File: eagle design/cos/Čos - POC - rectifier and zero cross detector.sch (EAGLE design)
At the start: 42 parts, among them IC1 LT1716CS5#TRMPBF, IC2 LBA710S, IC3 LBA710S, Q1 DMN10H220L-7

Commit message: - removed .net file from LTSpice simulation - updated schematics, generated BOM, ERC checks out fine
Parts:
- added C6: 4700μF / 35V / ultralow ESR, C-Pol:C-POL
- R10: device rcl:R-EU_R0402 -> rcl:R-EU_R0805
- R3, R4, R5, R6: value 3k795 -> 760R
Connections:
- net GND: now also C6.NEG
- net V_REGULATED_TP2-IN: now also C6.POS
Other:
- note added: "647-UPW1V472MHD - 4700uF/35V 647-UHD1V471MPD - 470uF/35V 647-UHD1V331MPD - 330uF/35V 647-UHD1V221MPD6 - 220uF/35V 647-UHV1V151MPD - 150uF/35V"
- note added: "Bicycle Dynamo Grätz Bridge Rectifier / Delon Voltage Doubler w. zero cross detector"
- note added: "Dynamo AC rectified & smoothed to: 0V>Vdc>18V"
- note added: "Grätz/Delon conceptual overview"
- note added: "LED resistors & jumpers for manual switch actuation"
- note added: "Load, conceptual overview"
- note added: "Solid-State Relay switches"
- note added: "Uf=1.2V, If=5mA R=(5V-1.2V)/5mA=3.8V/0.005A=760 Ohm"
- note added: "any load, ideally: Buck/Boost converter Vin:0-18V Vout:5V0"
- note added: "form A (NO); datasheet p. 3 LED current ~0.8mA, Uf=1.235V"
- note added: "form B (NC); datasheet p. 5 LED current ~0.23mA, Uf=1.235V"
- note added: "jumpers for switch bypass"
- note added: "switching elements, optically actuated MOSFets"
- note added: "zero-cross signal requires 5V0 input for level translation"
- note removed: "0V> Vdc > 18V"
- note removed: "5V0"
- note removed: "647-UHD1V471MPD - 470uF/35V 647-UHD1V331MPD - 330uF/35V 647-UHD1V221MPD6 - 220uF/35V 647-UHV1V151MPD - 150uF/35V"
- note removed: "AC Rectifier with zero cross detector"
- note removed: "Buck-Boost Converter Vin = regulated AC Vout = 5V0"
- note removed: "Capacitor switches"
- note removed: "Dynamo AC regulated output"
- note removed: "GND"
- note removed: "Load"
- note removed: "conceptual overview"
- moved on the sheet: C1, C2, C3, C4, C5, D1, D2, D3, D4, D5, D6, D7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

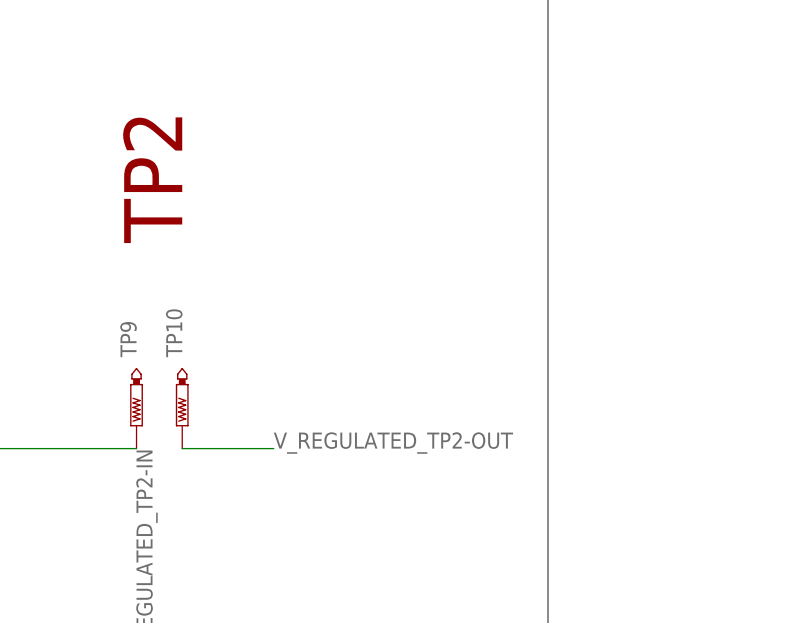
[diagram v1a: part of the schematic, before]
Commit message: - corrected netclasses
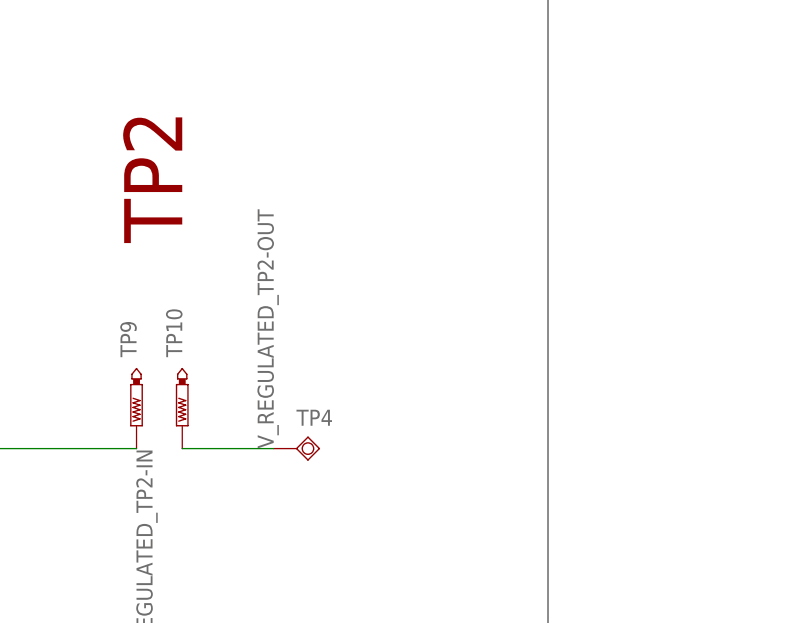
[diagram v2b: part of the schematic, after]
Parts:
- added TP4: Li-Ion Cell +, testpad:TPSQPAD1-13
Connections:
- net V_REGULATED_TP2-OUT: now also TP4.TP
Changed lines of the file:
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@@
 <clearance class="0" value="0.2"/>
 </class>
-<class number="1" name="GND_VIA_INCP" width="0.5" drill="0.3">
-<clearance class="1" value="0.2"/>
+<class number="1" name="DYNAMO_OUT" width="0.9" drill="0">
+<clearance class="1" value="0.5"/>
 </class>
-<class number="2" name="DYNAMO_OUT" width="0.9" drill="0.3">
-<clearance class="2" value="0.5"/>
+<class number="2" name="V_DC" width="0.3" drill="0.3">
+<clearance class="2" value="0.2"/>
 </class>
-<class number="3" name="V_DC" width="0.3" drill="0.3">
+<class number="3" name="V_REGULATED" width="0.3" drill="0.3">
 <clearance class="3" value="0.2"/>
 </class>
-<class number="4" name="V_REGULATED" width="0.3" drill="0.3">
+<class number="4" name="5V0" width="0.3" drill="0.3">
 <clearance class="4" value="0.2"/>
 </class>
-<class number="5" name="V_LI-ION" width="0.3" drill="0.3">
+<class number="5" name="signal" width="0.3" drill="0.3">
 <clearance class="5" value="0.2"/>
-</class>
-<class number="6" name="5V0" width="0.3" drill="0.3">
-<clearance class="6" value="0.2"/>
-</class>
-<class number="7" name="6V0" width="0.3" drill="0.3">
-<clearance class="7" value="0.2"/>
-</class>
-<class number="8" name="SOLAR-CELL" width="0.3" drill="0.3">
-<clearance class="8" value="0.2"/>
-</class>
-<class number="9" name="signal" width="0.3" drill="0.3">
-<clearance class="9" value="0.2"/>
-</class>
-<class number="10" name="LI_ION-CELL" width="0" drill="0">
 </class>
 </classes>
@@
 <part name="TP3" library="testpad" library_urn="urn:adsk.eagle:library:385" deviceset="TPSQ" device="PAD1-13" package3d_urn="urn:adsk.eagle:package:27946/1" value="Li-Ion Cell +"/>
 <part name="C6" library="C-Pol" deviceset="C-POL" device="" value="4700μF / 35V / ultralow ESR"/>
+<part name="TP4" library="testpad" library_urn="urn:adsk.eagle:library:385" deviceset="TPSQ" device="PAD1-13" package3d_urn="urn:adsk.eagle:package:27946/1" value="Li-Ion Cell +"/>
 </parts>
 <sheets>
@@
 <attribute name="VALUE" x="388.62" y="528.32" size="1.778" layer="96" rot="R90" align="center"/>
 </instance>
+<instance part="TP4" gate="G$1" x="429.26" y="548.64" smashed="yes" rot="R90">
+<attribute name="NAME" x="429.26" y="551.18" size="1.778" layer="95"/>
+<attribute name="TP_SIGNAL_NAME" x="430.53" y="551.18" size="1.778" layer="97" rot="R90"/>
+</instance>
 </instances>
 <busses>
@@
 </segment>
 </net>
-<net name="ZENER_COMMON" class="2">
+<net name="ZENER_COMMON" class="1">
 <segment>
 <pinref part="D2" gate="G$1" pin="C"/>
@@
 </segment>
 </net>
-<net name="DYNAMO2_GRAETZ" class="2">
+<net name="DYNAMO2_GRAETZ" class="1">
 <segment>
 <wire x1="218.44" y1="695.96" x2="218.44" y2="716.28" width="0.1524" layer="91"/>
@@
 </segment>
 </net>
-<net name="DYNAMO1" class="2">
+<net name="DYNAMO1" class="1">
 <segment>
 <pinref part="D4" gate="G$1" pin="C"/>
@@
 </segment>
 </net>
-<net name="DYNAMO2_BEFORE_TUNING-CAP_SW" class="2">
+<net name="DYNAMO2_BEFORE_TUNING-CAP_SW" class="1">
 <segment>
 <wire x1="152.4" y1="708.66" x2="144.78" y2="708.66" width="0.1524" layer="91"/>
@@
 </segment>
 </net>
-<net name="TUNING_CAP_BIAS" class="9">
+<net name="TUNING_CAP_BIAS" class="1">
 <segment>
 <pinref part="R10" gate="G$1" pin="1"/>
@@
 </segment>
 </net>
-<net name="DYNAMO2_DELON" class="2">
+<net name="DYNAMO2_DELON" class="1">
 <segment>
 <wire x1="289.56" y1="576.58" x2="279.4" y2="576.58" width="0.1524" layer="91"/>
@@
 <pinref part="TP10" gate="G$1" pin="TP"/>
 <wire x1="416.56" y1="548.64" x2="426.72" y2="548.64" width="0.1524" layer="91"/>
-<label x="426.72" y="548.64" size="1.778" layer="95"/>
+<label x="426.72" y="548.64" size="1.778" layer="95" rot="R90"/>
+<pinref part="TP4" gate="G$1" pin="TP"/>
 </segment>
 <segment>
@@
 </segment>
 </net>
-<net name="DYNAMO2_AFTER_TUNING-CAP_SW" class="2">
+<net name="DYNAMO2_AFTER_TUNING-CAP_SW" class="1">
 <segment>
 <wire x1="162.56" y1="708.66" x2="172.72" y2="708.66" width="0.1524" layer="91"/>
@@
 </segment>
 </net>
-<net name="DYNAMO2_BEFORE_G/D" class="2">
+<net name="DYNAMO2_BEFORE_G/D" class="1">
 <segment>
 <label x="190.5" y="716.28" size="0.8128" layer="95" rot="R90"/>
@@
 </segment>
 </net>
-<net name="ANODE_DELON" class="9">
+<net name="ANODE_DELON" class="5">
 <segment>
 <pinref part="IC3" gate="G$1" pin="3_ANODE2"/>
@@
 </segment>
 </net>
-<net name="ANODE_TUNING-CAP" class="9">
+<net name="ANODE_TUNING-CAP" class="5">
 <segment>
 <pinref part="IC2" gate="G$1" pin="3_ANODE2"/>
@@
 </segment>
 </net>
-<net name="ANODE_TUNING-CAP_BYPASS" class="9">
+<net name="ANODE_TUNING-CAP_BYPASS" class="5">
 <segment>
 <pinref part="IC2" gate="G$1" pin="1_ANODE1"/>
@@
 </segment>
 </net>
-<net name="ANODE_GRAETZ" class="9">
+<net name="ANODE_GRAETZ" class="5">
 <segment>
 <pinref part="IC3" gate="G$1" pin="1_ANODE1"/>
@@
 </segment>
 </net>
-<net name="OUT" class="0">
+<net name="OUT" class="5">
 <segment>
 <pinref part="IC1" gate="G$1" pin="1"/>
@@
 </segment>
 </net>
-<net name="ZEROCROSS" class="0">
+<net name="ZEROCROSS" class="5">
 <segment>
 <pinref part="Q1" gate="G$1" pin="S"/>
@@
 </segment>
 </net>
-<net name="5V0" class="0">
+<net name="5V0" class="4">
 <segment>
 <pinref part="Q1" gate="G$1" pin="G"/>
@@
 </segment>
 </net>
-<net name="N$4" class="0">
+<net name="N$4" class="5">
 <segment>
 <pinref part="R3" gate="G$1" pin="1"/>
@@
 </segment>
 </net>
-<net name="N$5" class="0">
+<net name="N$5" class="5">
 <segment>
 <pinref part="R4" gate="G$1" pin="1"/>
@@
 </segment>
 </net>
-<net name="N$6" class="0">
+<net name="N$6" class="5">
 <segment>
 <pinref part="R5" gate="G$1" pin="1"/>
@@
 </segment>
 </net>
-<net name="N$7" class="0">
+<net name="N$7" class="5">
 <segment>
 <pinref part="R6" gate="G$1" pin="1"/>

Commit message: - added SMD pads C-Pol.lbr library - 1st version of routed brd, ERC & DRC check out fine
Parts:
- added TP7, TP8: Li-Ion Cell +, testpad:TPSQPAD1-13
- C1, C2: value 330μF / 35V / ultralow ESR -> 3300μF / 35V / ultralow ESR; device C-Pol:C-POL -> C-Pol:C-POLSMD
- C3, C4: value 3300μF / 35V / ultralow ESR -> 330μF / 35V / ultralow ESR; device C-Pol:C-POL -> C-Pol:C-POLSMD
- C5, C6: device C-Pol:C-POL -> C-Pol:C-POLSMD
- TP1, TP2: value Li-Ion Cell + -> PTR1TP10SQ; device testpad:TPSQPAD1-13 -> testpad:PTR1TP10SQ
- TP10, TP9: value PTR1TP10SQ -> Li-Ion Cell +; device testpad:PTR1TP10SQ -> testpad:TPSQPAD1-13
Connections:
- net 5V0: now also JP5.1, JP6.1, TP7.TP; no longer JP1.1, JP2.1, TP3.TP
- net DYNAMO1: now also TP3.TP; no longer TP1.TP
- net DYNAMO2_AFTER_TUNING-CAP_SW: now also C1.NEG, JP2.1; no longer C3.NEG, JP6.1
- net DYNAMO2_BEFORE_G/D: now also C2.NEG, JP1.1; no longer C4.NEG, JP5.1
- net DYNAMO2_BEFORE_TUNING-CAP_SW: now also JP1.2, JP2.2, TP4.TP; no longer JP5.2, JP6.2, TP2.TP
- net DYNAMO2_DELON: now also C3.NEG, C4.POS; no longer C1.NEG, C2.POS
- net GND: now also C4.NEG, IC1.2_V-, TP10.TP; no longer C2.NEG, IC1.2
- net IN+: now also IC1.3_IN+; no longer IC1.3
- net IN-: now also IC1.4_IN-; no longer IC1.4
- net N$4: now also JP3.2; no longer JP1.2
- net N$5: now also JP4.2; no longer JP2.2
- net N$6: now also JP5.2; no longer JP3.2
- net N$7: now also JP6.2; no longer JP4.2
- net OUT: now also IC1.1_OUT; no longer IC1.1
- net TUNING_CAP_BIAS: now also C1.POS, C2.POS; no longer C3.POS, C4.POS
- net V_RECT_TP1-IN: now also C3.POS, TP1.TP; no longer C1.POS, TP5.TP
- net V_RECT_TP1-OUT: now also TP2.TP; no longer TP6.TP
- net V_REGULATED_TP2-IN: now also IC1.5_V+, TP5.TP; no longer IC1.5, TP9.TP
- net V_REGULATED_TP2-OUT: now also TP6.TP, TP9.TP; no longer TP10.TP, TP4.TP
- net ZEROCROSS: now also TP8.TP
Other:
- note added: "C5 / C6"
- note added: "D6"
- note removed: "C5"
- moved on the sheet: C1, C2, C3, C4, JP1, JP2, JP3, JP4, JP5, JP6, TP3, TP4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

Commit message: HW rev. 1 - finished routing, specified BOM, created gerbers
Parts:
- removed JP1, JP2, JP7, JP8: (no value), jumper:JP1Q
- added SW1_NC, SW2_NO, SW3_NC, SW4_NO: (no value), jumper:JP1Q
- renumbered JP3 to TCAP_BYPASS, JP4 to TCAP, JP5 to GRAETZ, JP6 to DELON, TP10 to GND, TP3 to DYN1, TP4 to DYN2, TP7 to 5V0, TP8 to ZC, TP9 to VREG
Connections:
- net DYNAMO2_AFTER_TUNING-CAP_SW: now also SW2_NO.1; no longer JP2.1
- net DYNAMO2_BEFORE_G/D: now also SW1_NC.1, SW3_NC.2, SW4_NO.2; no longer JP1.1, JP7.2, JP8.2
- net DYNAMO2_BEFORE_TUNING-CAP_SW: now also SW1_NC.2, SW2_NO.2; no longer JP1.2, JP2.2
- net DYNAMO2_DELON: now also SW4_NO.1; no longer JP8.1
- net DYNAMO2_GRAETZ: now also SW3_NC.1; no longer JP7.1
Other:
- note added: "647-UPW1V472MHD - 4700uF/35V 647-UHE1V332MHD6 - 3300uF/35V 647-UHD1V471MPD - 470uF/35V 647-UHD1V331MPD - 330uF/35V 647-UHD1V221MPD6 - 220uF/35V 647-UHV1V151MPD - 150uF/35V"
- note added: "jumpers for solid state relay override"
- note removed: "647-UPW1V472MHD - 4700uF/35V 647-UHD1V471MPD - 470uF/35V 647-UHD1V331MPD - 330uF/35V 647-UHD1V221MPD6 - 220uF/35V 647-UHV1V151MPD - 150uF/35V"
- note removed: "jumpers for switch bypass"

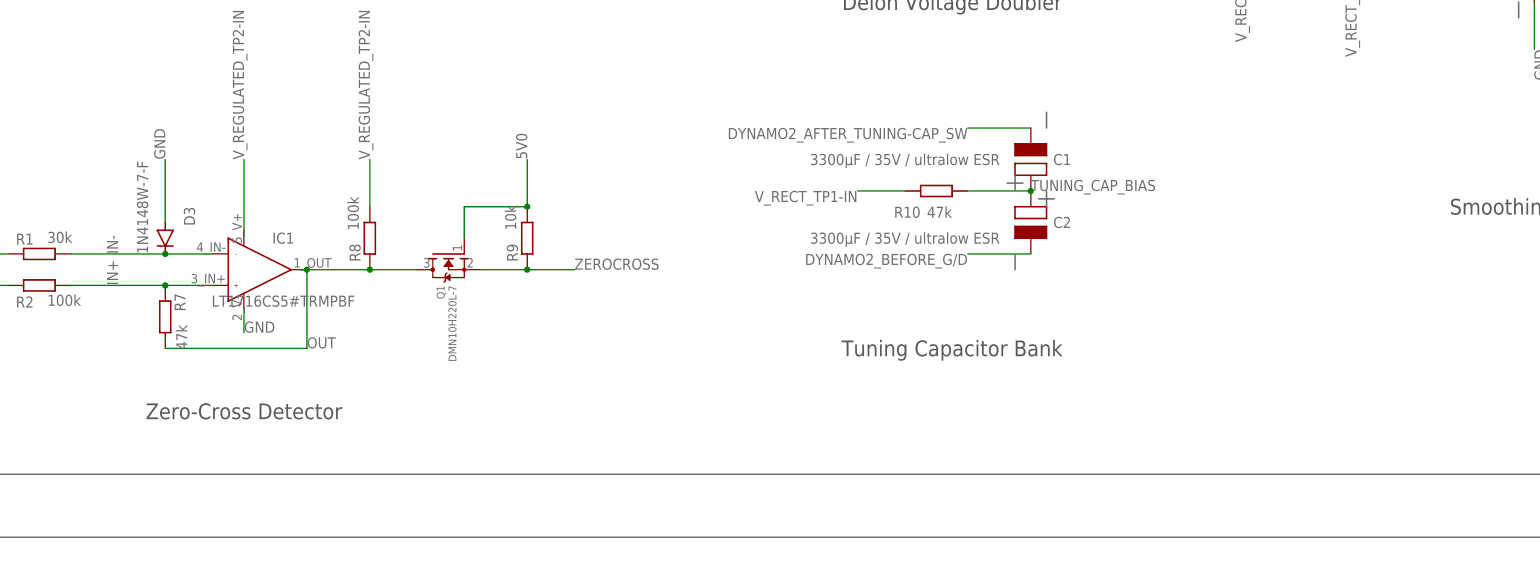
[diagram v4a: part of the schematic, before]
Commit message: - added passive bandpass filter to zero cross output
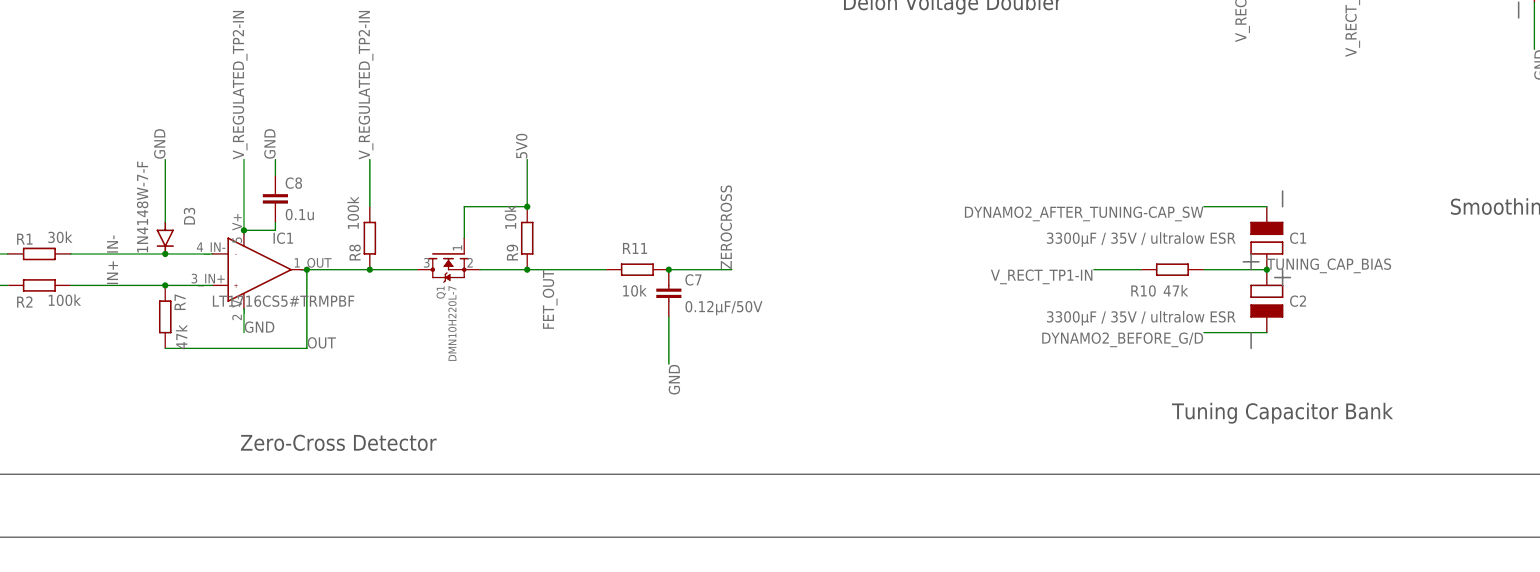
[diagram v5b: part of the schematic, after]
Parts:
- added C7: 0.12μF/50V, rcl:C-EUC0603
- added C8: 0.1u, rcl:C-EUC0603
- added R11: 10k, rcl:R-EU_R0805
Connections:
- new net FET_OUT: Q1.S, R11.1, R9.1
- net GND: now also C7.2, C8.1
- net V_REGULATED_TP2-IN: now also C8.2
- net ZEROCROSS: now also C7.1, R11.2; no longer Q1.S, R9.1
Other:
- note added: "band-pass filter"
- note added: "comparator circuitry"
- note added: "fcutoff = 132.7 Hz"
- note added: "voltage-level translation"
- moved on the sheet: C1, C2, R10

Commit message: - exchanged C-Pol from SMD to TH
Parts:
- removed C6: 4700μF / 35V / ultralow ESR, C-Pol:C-POLSMD
- C1, C2, C3, C4: device C-Pol:C-POLSMD -> C-Pol:C-POLTH
- C5: value 4700μF / 35V / ultralow ESR -> 2P 4700μF / 35V / ultralow ESR; device C-Pol:C-POLSMD -> C-Pol:C-POLTH
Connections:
- net GND: no longer C6.NEG
- net V_REGULATED_TP2-IN: no longer C6.POS

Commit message: - added solid state relay diode resistor calculation for 3.3V - renamed net 5V0 to VCC - moved output pins closer together % grouped them
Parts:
- renumbered 5V0 to VCC
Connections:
- net 5V0 renamed VCC
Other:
- note added: "R=(3.3V-1.2V)/5mA=2.1V/0.005A=420 Ohm"
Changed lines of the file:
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@@
 <clearance class="3" value="0.2"/>
 </class>
-<class number="4" name="5V0" width="0.3" drill="0.3">
+<class number="4" name="Vcc" width="0.3" drill="0.3">
 <clearance class="4" value="0.2"/>
 </class>
@@
 <part name="DYN2" library="testpad" library_urn="urn:adsk.eagle:library:385" deviceset="TPSQ" device="PAD1-13" package3d_urn="urn:adsk.eagle:package:27946/1" value="Li-Ion Cell +"/>
 <part name="ZC" library="testpad" library_urn="urn:adsk.eagle:library:385" deviceset="TPSQ" device="PAD1-13" package3d_urn="urn:adsk.eagle:package:27946/1" value="Li-Ion Cell +"/>
-<part name="5V0" library="testpad" library_urn="urn:adsk.eagle:library:385" deviceset="TPSQ" device="PAD1-13" package3d_urn="urn:adsk.eagle:package:27946/1" value="Li-Ion Cell +"/>
+<part name="VCC" library="testpad" library_urn="urn:adsk.eagle:library:385" deviceset="TPSQ" device="PAD1-13" package3d_urn="urn:adsk.eagle:package:27946/1" value="Li-Ion Cell +"/>
 <part name="GND" library="testpad" library_urn="urn:adsk.eagle:library:385" deviceset="TPSQ" device="PAD1-13" package3d_urn="urn:adsk.eagle:package:27946/1" value="Li-Ion Cell +"/>
 <part name="VREG" library="testpad" library_urn="urn:adsk.eagle:library:385" deviceset="TPSQ" device="PAD1-13" package3d_urn="urn:adsk.eagle:package:27946/1" value="Li-Ion Cell +"/>
@@
 <text x="127" y="525.78" size="1.27" layer="90" align="center">comparator circuitry</text>
 <text x="238.76" y="485.14" size="1.27" layer="90" align="center">fcutoff = 132.7 Hz</text>
+<text x="116.84" y="393.7" size="1.778" layer="97">R=(3.3V-1.2V)/5mA=2.1V/0.005A=420 Ohm</text>
 </plain>
 <instances>
@@
 <attribute name="TP_SIGNAL_NAME" x="441.96" y="697.23" size="1.778" layer="97"/>
 </instance>
-<instance part="5V0" gate="G$1" x="439.42" y="736.6" smashed="yes" rot="R180">
+<instance part="VCC" gate="G$1" x="439.42" y="736.6" smashed="yes" rot="R180">
 <attribute name="NAME" x="439.42" y="739.14" size="1.778" layer="95" rot="R90"/>
 <attribute name="TP_SIGNAL_NAME" x="436.88" y="737.87" size="1.778" layer="97" rot="R180"/>
@@
 </segment>
 </net>
-<net name="5V0" class="4">
+<net name="VCC" class="4">
 <segment>
 <pinref part="Q1" gate="G$1" pin="G"/>
@@
 <wire x1="439.42" y1="726.44" x2="439.42" y2="734.06" width="0.1524" layer="91"/>
 <label x="439.42" y="728.98" size="1.778" layer="95"/>
-<pinref part="5V0" gate="G$1" pin="TP"/>
-</segment>
-</net>
+<pinref part="VCC" gate="G$1" pin="TP"/>
+</segment>
+</net>

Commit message: - for LBA710 changed one pin direction to supply - added previously missing LT1716 Comparator.lbr - created LT1638 - Rail to Rail OpAmp.lbr & pdf - transferred ltspice schematic of peak detector & voltage follower into sch
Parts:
- added C10: 10nF, rcl:C-EUC0805
- added C6: 22nF, rcl:C-EUC0805
- added C9: 0.1u, rcl:C-EUC0805
- added D9: IN4148W, Diode:DIODE_IN4148W-TP_SOD123G
- added IC4: LT1638IDD#PBF, LT1638 - Rail to Rail OpAmp:LT1638
- added R12: 47k, rcl:R-EU_R0805
- added R13, R14, R16: 10k, rcl:R-EU_R0805
- added R15: 33R, rcl:R-EU_R0805
- added VF: Li-Ion Cell +, testpad:TPSQPAD1-13
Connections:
- new net A_IN+: C6.1, IC4.3_A_IN+, R14.2
- new net A_IN-: IC4.2_A_IN-, R16.2
- new net A_OUT: D9.A, IC4.1_A_OUT
- new net B_IN+: C10.1, IC4.5_B_IN+, R15.2, R16.1
- new net N$1: R12.2, R13.1, R14.1
- new net N$2: D9.C, R15.1
- new net VOLTAGEFOLLOWER: IC4.6_B_IN-, IC4.7_B_OUT, VF.TP
- net GND: now also C10.2, C6.2, C9.1, IC4.4_V-, R13.2
- net V_REGULATED_TP2-IN: now also C9.2, IC4.8_V+, R12.1
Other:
- note added: "Graetz Bridge"
- note added: "peak detector"
- note added: "peak detector & voltage follower"
- note added: "voltage follower"
- note added: "zero-cross signal requires 3V3 input for level translation"
- moved on the sheet: C3, C4, C5, D8, DELON, GRAETZ, IC2, IC3, R3, R4, R5, R6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
